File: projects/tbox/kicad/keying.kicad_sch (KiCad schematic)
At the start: 0 parts

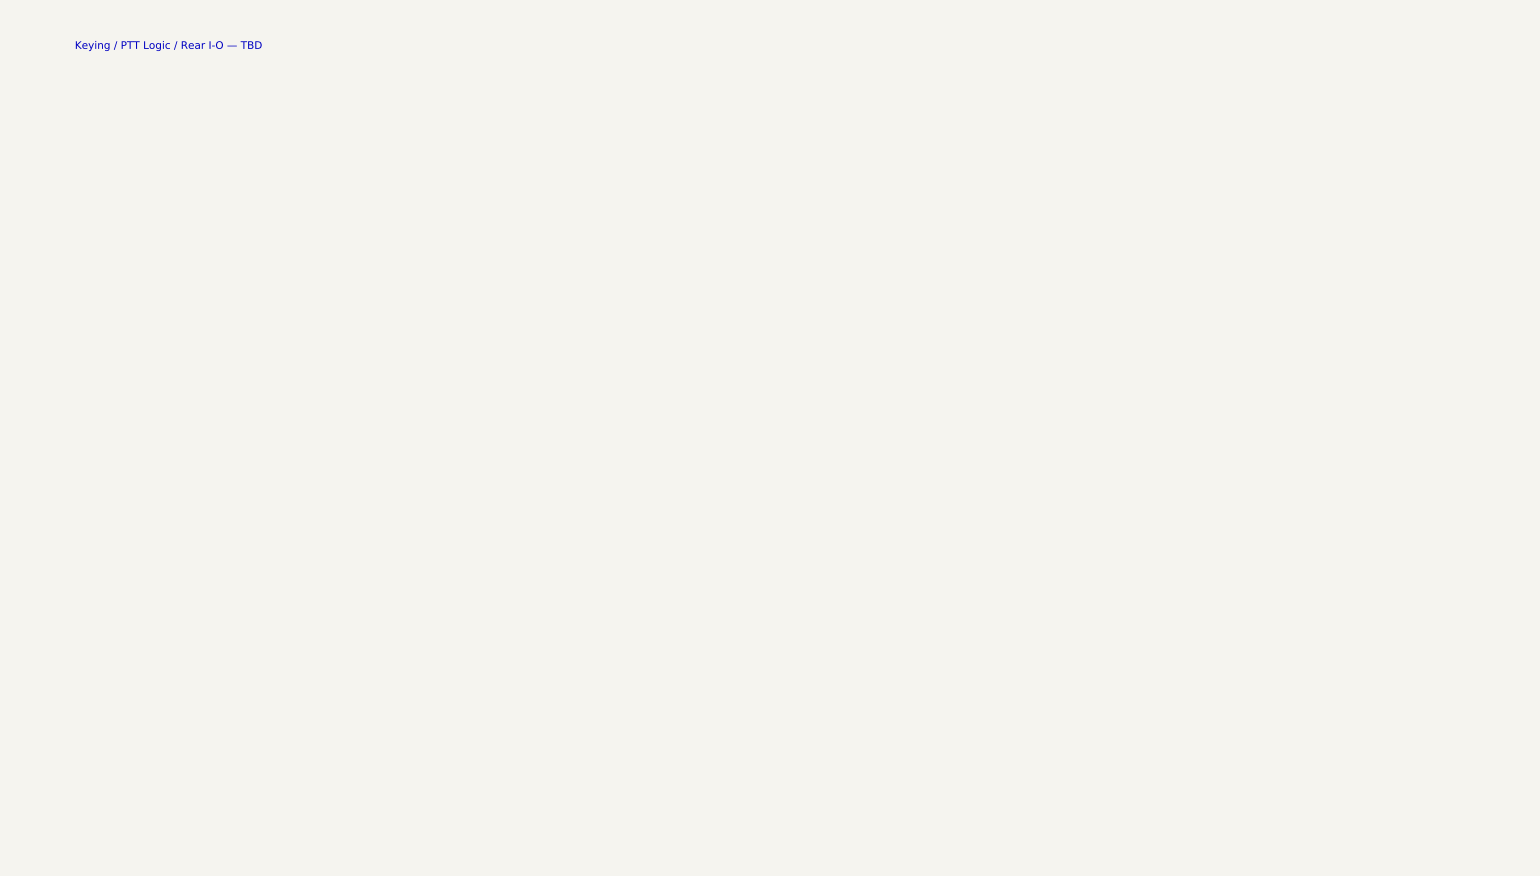
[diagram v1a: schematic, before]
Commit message: Complete the TX Bus, RX+Phones and Keying sheets; adversarial review fixes
Schematic
- New sheets: TX Bus (summing, intercom mute, mic/line out), RX + Phones,
  Keying + Rear (PTT, override, DE-9 with protection, indicators, rear
  switches, power-on mute hold).
- Mute is a shared sub-sheet (mute.kicad_sch) instanced in each preamp
  and the intercom.  Started as a JFET series+shunt pair; replaced by a
  TS12A12511 SPDT to VREF because a worst-case J113 is not pinched off
  inside the 9 V window at 0 dBV peaks.
- Preamp: TS12A12511 gain select (was DG419), HI +40 / LO +20 dB, RF
  entry filters, bias decoupling, feedback returns to GND.
- Supply: TPS7A4701 (ANY-OUT 9.0 V) replaces the LM2940, SMBJ18A input
  TVS, entry ceramics, VREF stiffened.
- VREF is DC bias only; every gain-setting leg returns to GND.
- CHASSIS net for all sleeves/returns with a single net tie; rear GND
  post; isolated line-out secondaries return to the jack sleeve.
- Keying logic transistors are 2N7002 so logic highs stay above ~7 V
  (the analog-switch VIH is 5 V guaranteed at 12 V); hold re-armed by a
  clamp diode.
- Test points on every sheet; title blocks rev 0.2.

Tooling and docs
- tools/check_sch.py: geometric lint for pins on wire interiors,
  touching pins, T-junctions without a dot, duplicate references.
- power_tree.json / Load_mA updated for the new regulator and loads.
- DESIGN.md, LEVELS.md, TODO.md brought in line (DRY trim, corrected
  numbers, open items); rear panel LINE L / LINE R.
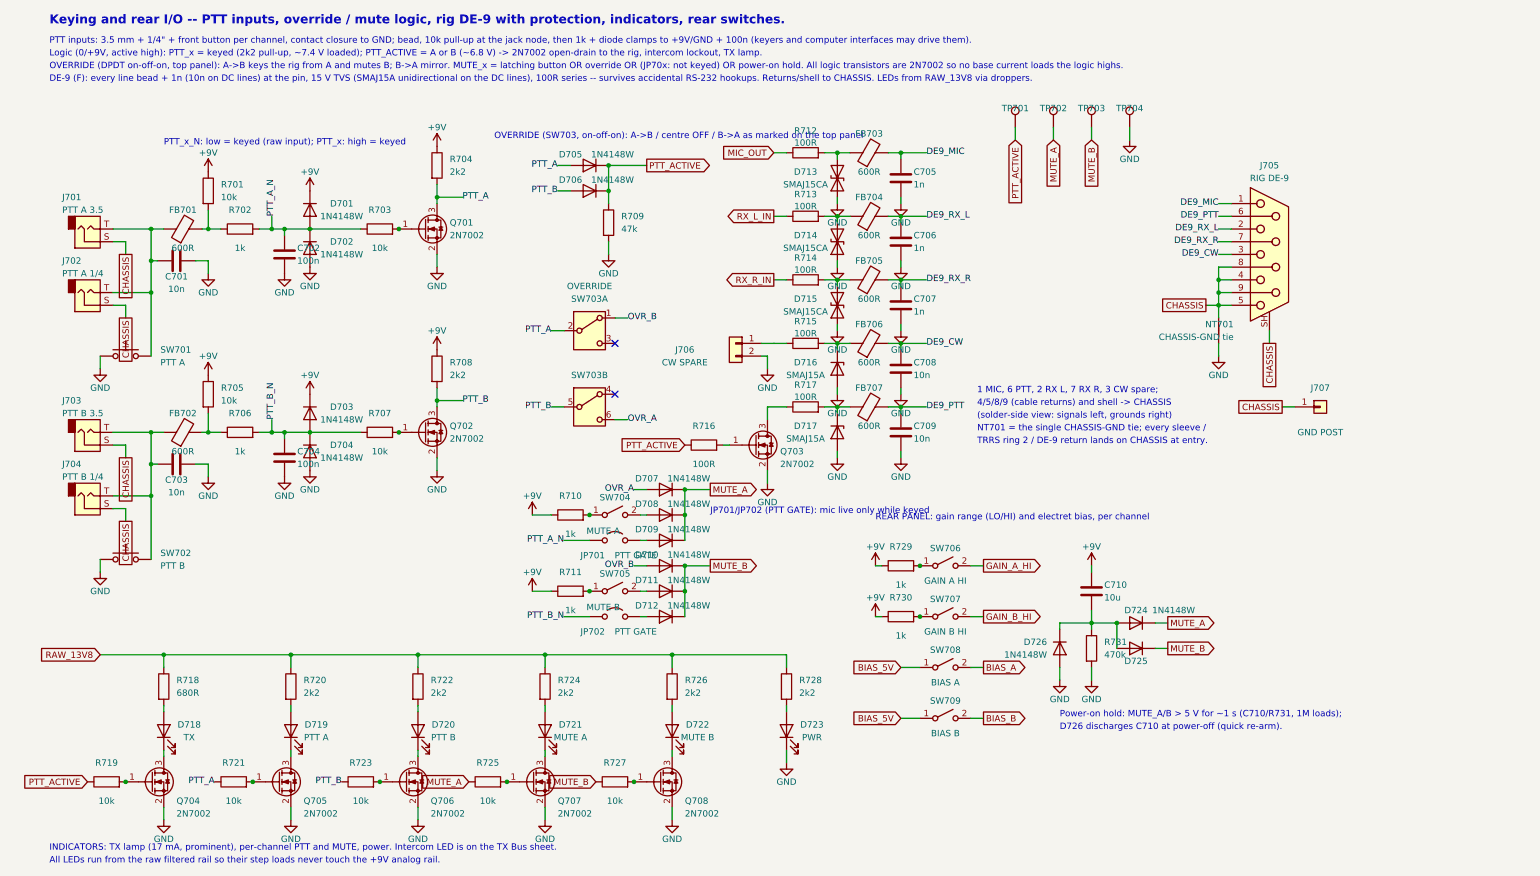
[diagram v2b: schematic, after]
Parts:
- added C701, C703, C708, C709: 10n, symbol Device:C
- added C702, C704: 100n, symbol Device:C
- added C705, C706, C707: 1n, symbol Device:C
- added C710: 10u, symbol Device:C
- added D701, D702, D703, D704, D705, D706, D707, D708, D709, D710, D711, D712, D724, D725, D726: 1N4148W, symbol tbox:1N4148W
- added D713, D714, D715: SMAJ15CA, symbol Device:D_TVS
- added D716, D717: SMAJ15A, symbol Device:D_Zener
- added D718: TX, symbol Device:LED
- added D719: PTT A, symbol Device:LED
- added D720: PTT B, symbol Device:LED
- added D721: MUTE A, symbol Device:LED
- added D722: MUTE B, symbol Device:LED
- added D723: PWR, symbol Device:LED
- added FB701, FB702, FB703, FB704, FB705, FB706, FB707: 600R, symbol Device:FerriteBead
- added J701: PTT A 3.5, symbol Connector_Audio:AudioJack2
- added J702: PTT A 1/4, symbol Connector_Audio:AudioJack2
- added J703: PTT B 3.5, symbol Connector_Audio:AudioJack2
- added J704: PTT B 1/4, symbol Connector_Audio:AudioJack2
- added J705: RIG DE-9, symbol Connector:DE9_Socket_MountingHoles
- added J706: CW SPARE, symbol Connector_Generic:Conn_01x02
- added J707: GND POST, symbol Connector_Generic:Conn_01x01
- added JP701, JP702: PTT GATE, symbol Jumper:Jumper_2_Open
- added NT701: CHASSIS-GND tie, symbol Device:NetTie_2
- added Q701, Q702, Q703, Q704, Q705, Q706, Q707, Q708: 2N7002, symbol tbox:2N7002
- added R701, R703, R705, R707, R719, R721, R723, R725, R727: 10k, symbol Device:R
- added R702, R706, R710, R711, R729, R730: 1k, symbol Device:R
- added R704, R708, R720, R722, R724, R726, R728: 2k2, symbol Device:R
- added R709: 47k, symbol Device:R
- added R712, R713, R714, R715, R716, R717: 100R, symbol Device:R
- added R718: 680R, symbol Device:R
- added R731: 470k, symbol Device:R
- added SW701: PTT A, symbol Switch:SW_Push
- added SW702: PTT B, symbol Switch:SW_Push
- added SW703: OVERRIDE, symbol Switch:SW_DPDT_x2
- added SW704: MUTE A, symbol Switch:SW_SPST
- added SW705: MUTE B, symbol Switch:SW_SPST
- added SW706: GAIN A HI, symbol Switch:SW_SPST
- added SW707: GAIN B HI, symbol Switch:SW_SPST
- added SW708: BIAS A, symbol Switch:SW_SPST
- added SW709: BIAS B, symbol Switch:SW_SPST
- added TP701: PTT_ACTIVE, symbol Connector:TestPoint
- added TP702: MUTE_A, symbol Connector:TestPoint
- added TP703: MUTE_B, symbol Connector:TestPoint
- added TP704: GND, symbol Connector:TestPoint
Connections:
- new net: C701.1, FB701.1, J701.T, J702.T, SW701.2
- new net: FB701.2, R701.2, R702.1
- new net: Q706.1 (G), R723.2
- new net: D708.2 (A), SW704.2 (B)
- new net: D712.2 (A), JP702.2 (B)
- new net: R729.2, SW706.1 (A)
- new net: D714.2 (A2), FB704.1, R713.2
- new net: Q704.1 (G), R719.2
- new net: D718.1 (K), Q704.3 (D)
- new net: Q707.1 (G), R725.2
- new net: D718.2 (A), R718.2
- new net: R710.2, SW704.1 (A)
- new net: C710.2, D724.2 (A), D725.2 (A), D726.1 (K), R731.1
- new net: J706.1 (Pin_1), R715.1
- new net: D716.1 (K), FB706.1, R715.2
- new net: D713.2 (A2), FB703.1, R712.2
- new net: D721.2 (A), R724.2
- new net: R711.2, SW705.1 (A)
- new net: D711.2 (A), SW705.2 (B)
- new net: D719.1 (K), Q705.3 (D)
- new net: D719.2 (A), R720.2
- new net: D709.2 (A), JP701.2 (B)
- new net: D722.1 (K), Q708.3 (D)
- new net: D722.2 (A), R726.2
- new net: Q702.1 (G), R707.2
- new net: D717.1 (K), FB707.1, R717.2
- new net: FB702.2, R705.2, R706.1
- new net: C703.1, FB702.1, J703.T, J704.T, SW702.2
- new net: Q708.1 (G), R727.2
- new net: D720.1 (K), Q706.3 (D)
- new net: Q701.1 (G), R703.2
- new net: Q705.1 (G), R721.2
- new net: R730.2, SW707.1 (A)
- new net: D720.2 (A), R722.2
- new net: D715.2 (A2), FB705.1, R714.2
- new net: Q703.1 (G), R716.2
- new net: D721.1 (K), Q707.3 (D)
- new net: Q703.3 (D), R717.1
- new net: D723.2 (A), R728.2
- new net +9V: C710.1, D701.1 (K), D703.1 (K), R701.1, R704.1, R705.1, R708.1, R710.1, R711.1, R729.1, R730.1
- new net BIAS_5V: SW708.1 (A), SW709.1 (A)
- new net BIAS_A: SW708.2 (B)
- new net BIAS_B: SW709.2 (B)
- new net CHASSIS: J701.S, J702.S, J703.S, J704.S, J705.4, J705.5, J705.8, J705.9, J705.SH (PAD), J707.1 (Pin_1), NT701.2
- new net DE9_CW: C708.1, FB706.2, J705.3
- new net DE9_MIC: C705.1, FB703.2, J705.1
- new net DE9_PTT: C709.1, FB707.2, J705.6
- new net DE9_RX_L: C706.1, FB704.2, J705.2
- new net DE9_RX_R: C707.1, FB705.2, J705.7
- new net GAIN_A_HI: SW706.2 (B)
- new net GAIN_B_HI: SW707.2 (B)
- new net GND: C701.2, C702.2, C703.2, C704.2, C705.2, C706.2, C707.2, C708.2, C709.2, D702.2 (A), D704.2 (A), D713.1 (A1), D714.1 (A1), D715.1 (A1), D716.2 (A), D717.2 (A), D723.1 (K), D726.2 (A), J706.2 (Pin_2), NT701.1, Q701.2 (S), Q702.2 (S), Q703.2 (S), Q704.2 (S), Q705.2 (S), Q706.2 (S), Q707.2 (S), Q708.2 (S), R709.2, R731.2, SW701.1, SW702.1, TP704.1
- new net MIC_OUT: R712.1
- new net MUTE_A: D707.1 (K), D708.1 (K), D709.1 (K), D724.1 (K), R725.1, TP702.1
- new net MUTE_B: D710.1 (K), D711.1 (K), D712.1 (K), D725.1 (K), R727.1, TP703.1
- new net OVR_A: D707.2 (A), SW703.6 (C)
- new net OVR_B: D710.2 (A), SW703.1 (A)
- new net PTT_A: D705.2 (A), Q701.3 (D), R704.2, R721.1, SW703.2 (B)
- new net PTT_ACTIVE: D705.1 (K), D706.1 (K), R709.1, R716.1, R719.1, TP701.1
- new net PTT_A_N: C702.1, D701.2 (A), D702.1 (K), JP701.1 (A), R702.2, R703.1
- new net PTT_B: D706.2 (A), Q702.3 (D), R708.2, R723.1, SW703.5 (B)
- new net PTT_B_N: C704.1, D703.2 (A), D704.1 (K), JP702.1 (A), R706.2, R707.1
- new net RAW_13V8: R718.1, R720.1, R722.1, R724.1, R726.1, R728.1
- new net RX_L_IN: R713.1
- new net RX_R_IN: R714.1
- no-connect marks 0 -> 2
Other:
- note added: "(solder-side view: signals left, grounds right)"
- note added: "1 MIC, 6 PTT, 2 RX L, 7 RX R, 3 CW spare;"
- note added: "4/5/8/9 (cable returns) and shell -> CHASSIS"
- note added: "All LEDs run from the raw filtered rail so their step loads never touch the +9V analog rail."
- note added: "D726 discharges C710 at power-off (quick re-arm)."
- note added: "DE-9 (F): every line bead + 1n (10n on DC lines) at the pin, 15 V TVS (SMAJ15A unidirectional on the DC lines), 100R series -- survives accidental RS-232 hookups. Returns/shell to CHASSIS. LEDs from RAW_13V8 via droppers."
- note added: "INDICATORS: TX lamp (17 mA, prominent), per-channel PTT and MUTE, power. Intercom LED is on the TX Bus sheet."
- note added: "JP701/JP702 (PTT GATE): mic live only while keyed"
- note added: "Keying and rear I/O -- PTT inputs, override / mute logic, rig DE-9 with protection, indicators, rear switches."
- note added: "Logic (0/+9V, active high): PTT_x = keyed (2k2 pull-up, ~7.4 V loaded); PTT_ACTIVE = A or B (~6.8 V) -> 2N7002 open-drain to the rig, intercom lockout, TX lamp."
- note added: "NT701 = the single CHASSIS-GND tie; every sleeve /"
- note added: "OVERRIDE (DPDT on-off-on, top panel): A->B keys the rig from A and mutes B; B->A mirror. MUTE_x = latching button OR override OR (JP70x: not keyed) OR power-on hold. All logic transistors are 2N7002 so no base current loads the logic highs."
- note added: "OVERRIDE (SW703, on-off-on): A->B / centre OFF / B->A as marked on the top panel"
- note added: "PTT inputs: 3.5 mm + 1/4" + front button per channel, contact closure to GND; bead, 10k pull-up at the jack node, then 1k + diode clamps to +9V/GND + 100n (keyers and computer interfaces may drive them)."
- note added: "PTT_x_N: low = keyed (raw input); PTT_x: high = keyed"
- note added: "Power-on hold: MUTE_A/B > 5 V for ~1 s (C710/R731, 1M loads);"
- note added: "REAR PANEL: gain range (LO/HI) and electret bias, per channel"
- note added: "TRRS ring 2 / DE-9 return lands on CHASSIS at entry."
- note removed: "Keying / PTT Logic / Rear I-O — TBD"
- title: TBox — Keying / PTT Logic / Rear I-O -> TBox — Keying / Rear I/O

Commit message: Replace NE5532 with OPA1678; annotate logic pull-up loads
The NE5532 is only specified from 10 V total; at 9 V its input
common-mode range works out to 3-6 V (0.1 V of margin at 0 dBV peaks)
and TI no longer specifies its output swing at all.  The OPA1678 is
pin-compatible, specified 4.5-36 V, guarantees the output within 0.8 V
of each rail and a 0.5-7 V input range, has slightly lower noise
(4.5 nV/rtHz) and draws 2 mA/ch instead of up to 8.

- tbox.kicad_sym: OPA1678 symbol replaces NE5532 (all 8 packages).
- Load_mA 4/5 per package, including the previously unannotated
  preamps; PTT inverter pull-ups, mute buttons and the intercom NOR
  are now annotated too (they were the missing "discretes").
- power_tree.json: +9V budget 60 typ / 175 max (was 70/205), Pd note;
  extracted loads now reconcile exactly (174 mA max, 17 parts).
- LEVELS: clip point +8 dBV guaranteed, plan still budgets +6.
  DESIGN/TODO updated; the "measure the 5532 clip" bench item is gone.
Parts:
- R704, R708: Load_mA (none) -> 4
- R710, R711: Load_mA (none) -> 0/8
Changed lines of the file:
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@@
     (property "Reference" "R704" (at 100.33 46.99 0) (effects (font (size 1.27 1.27)) (justify left)))
     (property "Value" "2k2" (at 100.33 49.53 0) (effects (font (size 1.27 1.27)) (justify left)))
+    (property "Load_mA" "4" (at 100.33 46.99 0) (effects (font (size 1.27 1.27)) (hide yes)))
     (property "Footprint" "" (at 97.79 48.26 0) (effects (font (size 1.27 1.27)) (hide yes)))
     (property "Datasheet" "" (at 97.79 48.26 0) (effects (font (size 1.27 1.27)) (hide yes)))
@@
     (property "Reference" "R708" (at 100.33 87.63 0) (effects (font (size 1.27 1.27)) (justify left)))
     (property "Value" "2k2" (at 100.33 90.17 0) (effects (font (size 1.27 1.27)) (justify left)))
+    (property "Load_mA" "4" (at 100.33 87.63 0) (effects (font (size 1.27 1.27)) (hide yes)))
     (property "Footprint" "" (at 97.79 88.9 0) (effects (font (size 1.27 1.27)) (hide yes)))
     (property "Datasheet" "" (at 97.79 88.9 0) (effects (font (size 1.27 1.27)) (hide yes)))
@@
     (property "Reference" "R710" (at 124.46 114.3 90) (effects (font (size 1.27 1.27))))
     (property "Value" "1k" (at 124.46 121.92 90) (effects (font (size 1.27 1.27))))
+    (property "Load_mA" "0/8" (at 124.46 114.3 0) (effects (font (size 1.27 1.27)) (hide yes)))
     (property "Footprint" "" (at 124.46 118.11 0) (effects (font (size 1.27 1.27)) (hide yes)))
     (property "Datasheet" "" (at 124.46 118.11 0) (effects (font (size 1.27 1.27)) (hide yes)))
@@
     (property "Reference" "R711" (at 124.46 129.54 90) (effects (font (size 1.27 1.27))))
     (property "Value" "1k" (at 124.46 137.16 90) (effects (font (size 1.27 1.27))))
+    (property "Load_mA" "0/8" (at 124.46 129.54 0) (effects (font (size 1.27 1.27)) (hide yes)))
     (property "Footprint" "" (at 124.46 133.35 0) (effects (font (size 1.27 1.27)) (hide yes)))
     (property "Datasheet" "" (at 124.46 133.35 0) (effects (font (size 1.27 1.27)) (hide yes)))

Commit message: Power tree: topology and loads from the schematic, capability from json
power_tree.json now holds only what the schematic cannot know: per-rail
max_ma, its basis and derivation, thresholds.  tools/power_model.py
derives the rail tree from converter pins (power_in -> power_out, or a
Rail_out field where the output reaches the rail through a passive or a
plain output pin) and collects Load_mA per part; both check_power.py
and gen_power_tree.py build on it.

- Rails are flattened: every load is an occurrence on its own rail and
  on each rail upstream (1:1 through linear stages; efficiency + v for
  a switching stage).  RAW_13V8 now reads 68/298 mA rather than the
  48 mA of its direct loads.
- typ/max convention written down (CLAUDE.md, power_model.py); LEDs and
  the intercom NOR annotated as 0/x; phones amps re-rated for the 16 ohm
  headsets LEVELS specifies (10/90 per package, was the 32 ohm 10/53).
  +9V is 62 typ / 250 max, 65 % of the 385 mA thermal cap -- which the
  layout has to earn (TODO records the 2-layer ~250 mA figure).
- Electret bias feeds annotated; VREF declared no_loads by design;
  Rail_out on U2 (RC after VOUT) and U3 (op-amp buffer).
- Tree boxes size to their text; supply-sheet notes get the measured
  load line prepended and were moved off the parts.
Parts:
- R718: Load_mA 17 -> 0/17
- R720, R722, R724, R726: Load_mA 5 -> 0/5
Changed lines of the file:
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@@
     (property "Datasheet" "" (at 43.18 152.4 0) (effects (font (size 1.27 1.27)) (hide yes)))
     (property "Description" "" (at 43.18 152.4 0) (effects (font (size 1.27 1.27)) (hide yes)))
-    (property "Load_mA" "17" (at 43.18 152.4 0) (effects (font (size 1.27 1.27)) (hide yes)))
+    (property "Load_mA" "0/17" (at 43.18 152.4 0) (effects (font (size 1.27 1.27)) (hide yes)))
     (pin "1")
     (pin "2")
@@
     (property "Datasheet" "" (at 68.58 152.4 0) (effects (font (size 1.27 1.27)) (hide yes)))
     (property "Description" "" (at 68.58 152.4 0) (effects (font (size 1.27 1.27)) (hide yes)))
-    (property "Load_mA" "5" (at 68.58 152.4 0) (effects (font (size 1.27 1.27)) (hide yes)))
+    (property "Load_mA" "0/5" (at 68.58 152.4 0) (effects (font (size 1.27 1.27)) (hide yes)))
     (pin "1")
     (pin "2")
@@
     (property "Datasheet" "" (at 93.98 152.4 0) (effects (font (size 1.27 1.27)) (hide yes)))
     (property "Description" "" (at 93.98 152.4 0) (effects (font (size 1.27 1.27)) (hide yes)))
-    (property "Load_mA" "5" (at 93.98 152.4 0) (effects (font (size 1.27 1.27)) (hide yes)))
+    (property "Load_mA" "0/5" (at 93.98 152.4 0) (effects (font (size 1.27 1.27)) (hide yes)))
     (pin "1")
     (pin "2")
@@
     (property "Datasheet" "" (at 119.38 152.4 0) (effects (font (size 1.27 1.27)) (hide yes)))
     (property "Description" "" (at 119.38 152.4 0) (effects (font (size 1.27 1.27)) (hide yes)))
-    (property "Load_mA" "5" (at 119.38 152.4 0) (effects (font (size 1.27 1.27)) (hide yes)))
+    (property "Load_mA" "0/5" (at 119.38 152.4 0) (effects (font (size 1.27 1.27)) (hide yes)))
     (pin "1")
     (pin "2")
@@
     (property "Datasheet" "" (at 144.78 152.4 0) (effects (font (size 1.27 1.27)) (hide yes)))
     (property "Description" "" (at 144.78 152.4 0) (effects (font (size 1.27 1.27)) (hide yes)))
-    (property "Load_mA" "5" (at 144.78 152.4 0) (effects (font (size 1.27 1.27)) (hide yes)))
-    (pin "1")
-    (pin "2")
+    (property "Load_mA" "0/5" (at 144.78 152.4 0) (effects (font (size 1.27 1.27)) (hide yes)))
+    (pin "1")
+    (pin "2")
